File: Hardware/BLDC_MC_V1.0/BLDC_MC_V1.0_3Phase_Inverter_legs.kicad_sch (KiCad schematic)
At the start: 30 parts, among them Q1 BSC027N10NS5ATMA1, Q2 BSC027N10NS5ATMA1, Q3 BSC027N10NS5ATMA1, Q4 BSC027N10NS5ATMA1, Q5 BSC027N10NS5ATMA1, Q6 BSC027N10NS5ATMA1

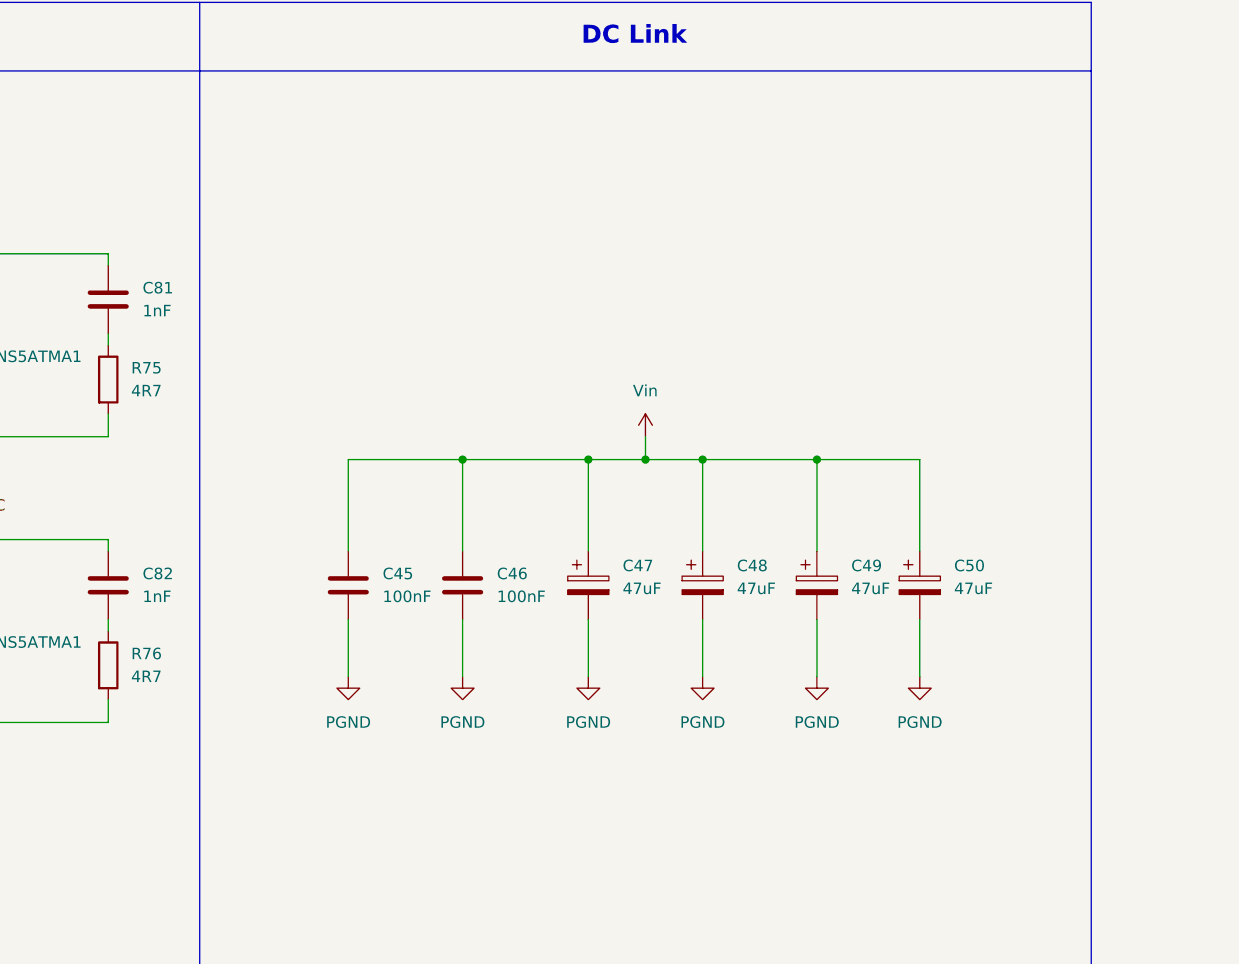
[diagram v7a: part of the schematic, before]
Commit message: Add notes about how to adjust the snubber circuit
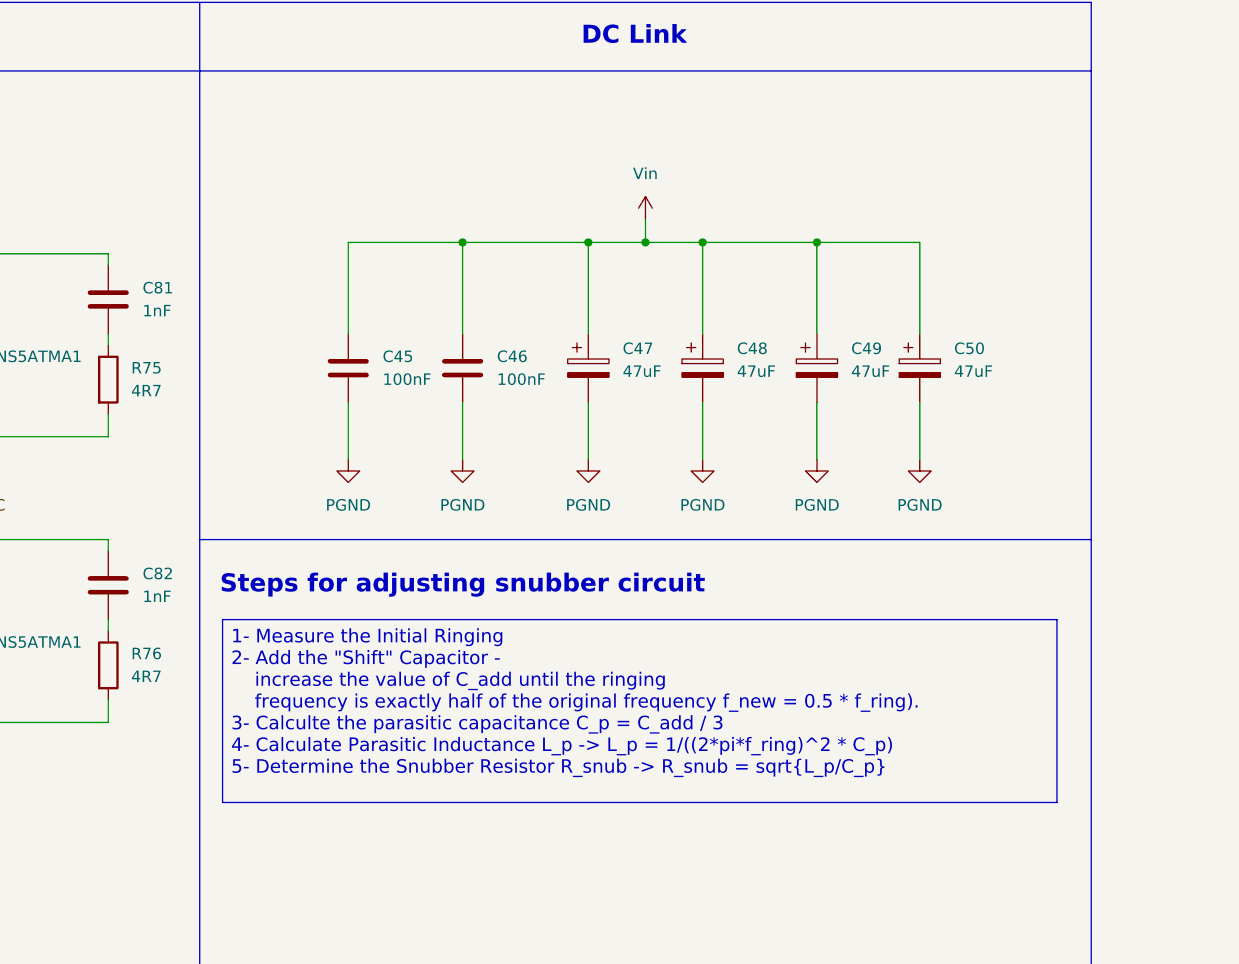
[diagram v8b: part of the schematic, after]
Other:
- note added: "Steps for adjusting snubber circuit"
- moved on the sheet: C45, C46, C47, C48, C49, C50
